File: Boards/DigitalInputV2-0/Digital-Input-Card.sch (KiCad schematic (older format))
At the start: 42 parts, among them IC1 PIC32MM0064GPM028, P1 1x6 2.54 Pin Header, P2 1x12 2.54, P3 1x2 2.54, P4 1x4 2.54, P5 Stacked USBA, Q1 AO3407A, Q2 NX7002AK, Q3 NX7002AK, Q4 NX7002AK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

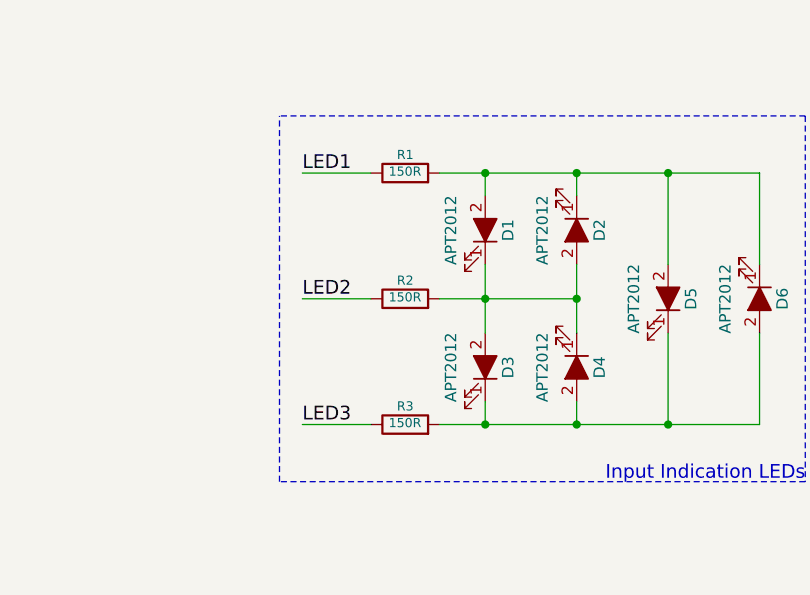
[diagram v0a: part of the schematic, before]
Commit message: worked on charlieplexed led circuit design
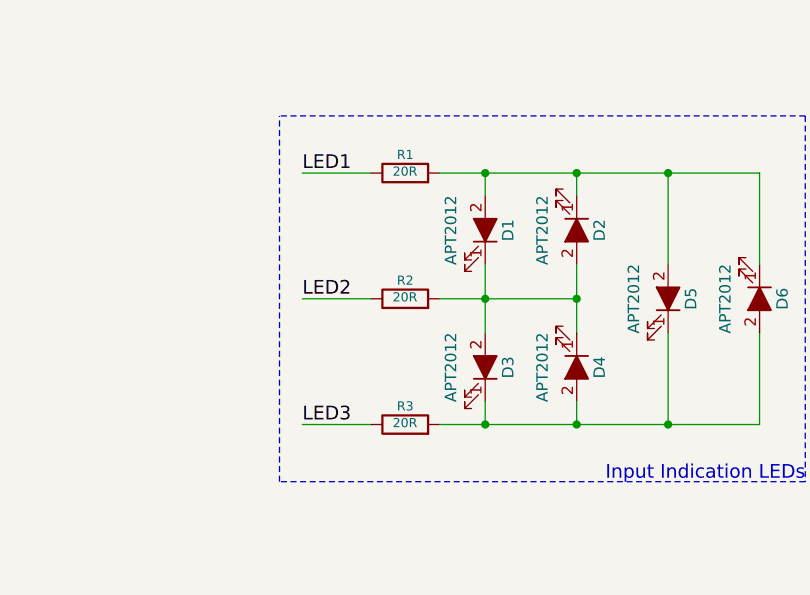
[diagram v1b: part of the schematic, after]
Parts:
- R1, R2, R3: value 150R -> 20R
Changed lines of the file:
@@
 P 7550 2100
 F 0 "R2" V 7630 2100 40  0000 C CNN
-F 1 "150R" V 7557 2101 40  0000 C CNN
+F 1 "20R" V 7557 2101 40  0000 C CNN
 F 2 "Resistors_SMD:R_0805" V 7480 2100 30  0001 C CNN
 F 3 "~" H 7550 2100 30  0000 C CNN
@@
 P 7550 2650
 F 0 "R3" V 7630 2650 40  0000 C CNN
-F 1 "150R" V 7557 2651 40  0000 C CNN
+F 1 "20R" V 7557 2651 40  0000 C CNN
 F 2 "Resistors_SMD:R_0805" V 7480 2650 30  0001 C CNN
 F 3 "~" H 7550 2650 30  0000 C CNN
@@
 P 7550 1550
 F 0 "R1" V 7630 1550 40  0000 C CNN
-F 1 "150R" V 7557 1551 40  0000 C CNN
+F 1 "20R" V 7557 1551 40  0000 C CNN
 F 2 "Resistors_SMD:R_0805" V 7480 1550 30  0001 C CNN
 F 3 "~" H 7550 1550 30  0000 C CNN
